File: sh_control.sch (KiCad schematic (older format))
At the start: 0 parts

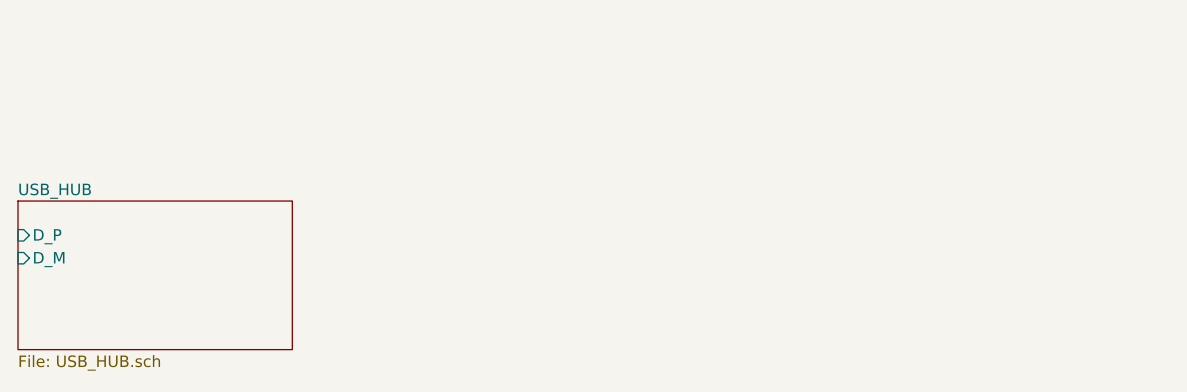
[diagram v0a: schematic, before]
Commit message: added atmega32 schematic
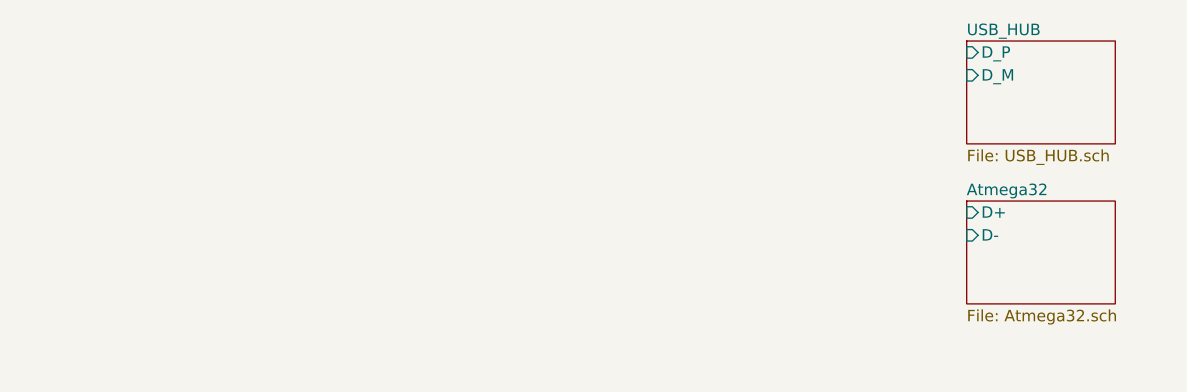
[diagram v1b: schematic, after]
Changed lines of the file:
@@
 $Descr A4 11693 8268
 encoding utf-8
-Sheet 1 2
+Sheet 1 3
 Title ""
 Date ""
@@
 $EndDescr
 $Sheet
-S 1800 2400 1200 650
+S 5950 1700 650  450
 U 61280420
 F0 "USB_HUB" 50
 F1 "USB_HUB.sch" 50
-F2 "D_P" I L 1800 2550 50
-F3 "D_M" I L 1800 2650 50
+F2 "D_P" I L 5950 1750 50
+F3 "D_M" I L 5950 1850 50
+$EndSheet
+$Sheet
+S 5950 2400 650  450
+U 61383560
+F0 "Atmega32" 50
+F1 "Atmega32.sch" 50
+F2 "D+" I L 5950 2450 50
+F3 "D-" I L 5950 2550 50
 $EndSheet
 $EndSCHEMATC

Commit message: file: finished schematic
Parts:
- added C19, C? (x4): 100 uF, symbol Device:C_Small
- added D10, D11, D12, D13, D14: WS2812B, LED_SMD:LED_WS2812B_PLCC4_5.0x5.0mm_P3.2mm, symbol LED:WS2812B
- added D15: LED_Small, symbol Device:LED_Small
- added F1: 500 mA, symbol Device:Fuse
- added J6: C10418, C10418, symbol max_KiCAD_lib:C10418
- added R14: 1.5K, symbol Device:R_Small
- added R?: 300, symbol Device:R_Small
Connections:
- new net: F1.2, J6.1
- new net: D15.2 (A), R14.2
- new net: D10.2 (DOUT), D11.4 (DIN)
- new net: D10.4 (DIN), R?.1
- new net: C?.1, D11.1 (VDD)
- new net: D11.2 (DOUT), D12.4 (DIN)
- new net: C?.1, D13.1 (VDD)
- new net: D13.2 (DOUT), D14.4 (DIN)
- new net: D12.2 (DOUT), D13.4 (DIN)
- new net: C?.1, D14.1 (VDD)
- new net: C?.1, D12.1 (VDD)
- new net +5V: C19.1, D10.1 (VDD), F1.1, R14.1
- new net D_N: J6.2
- new net D_P: J6.3
- new net GND: C19.2, C?.2, C?.2, C?.2, C?.2, D10.3 (VSS), D11.3 (VSS), D12.3 (VSS), D13.3 (VSS), D14.3 (VSS), D15.1 (K), J6.5, J6.6 (MH1), J6.7 (MH2), J6.8 (MH3), J6.9 (MH4)
- new net data: R?.2
- no-connect marks 0 -> 1

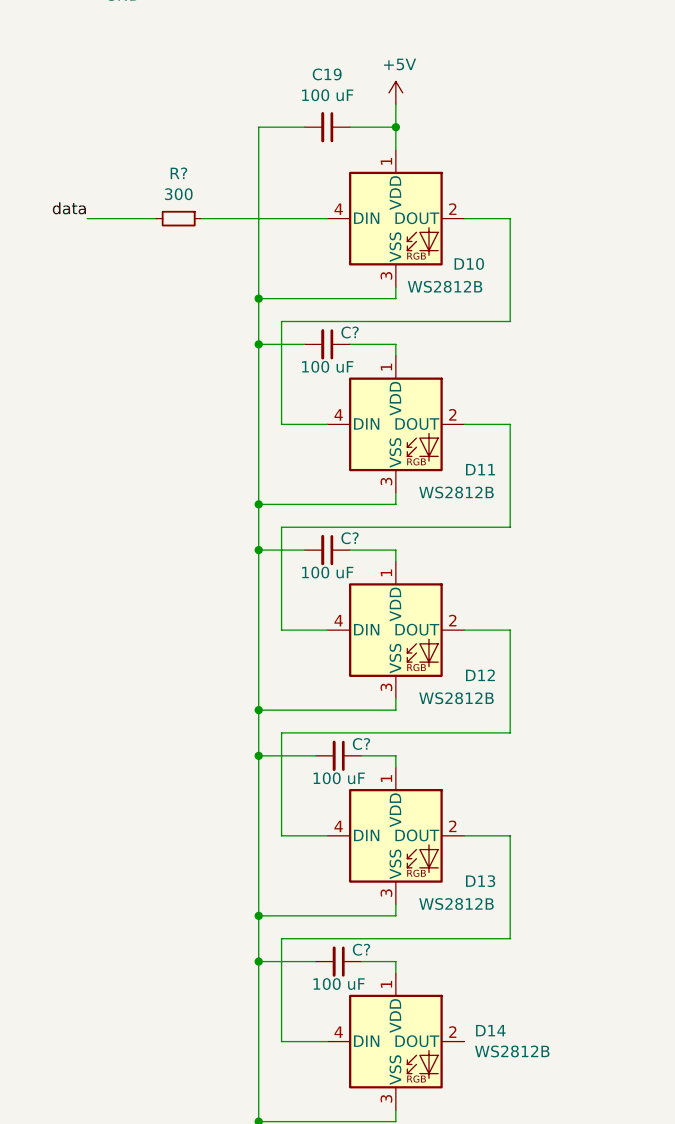
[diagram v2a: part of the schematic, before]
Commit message: small changes to schematic
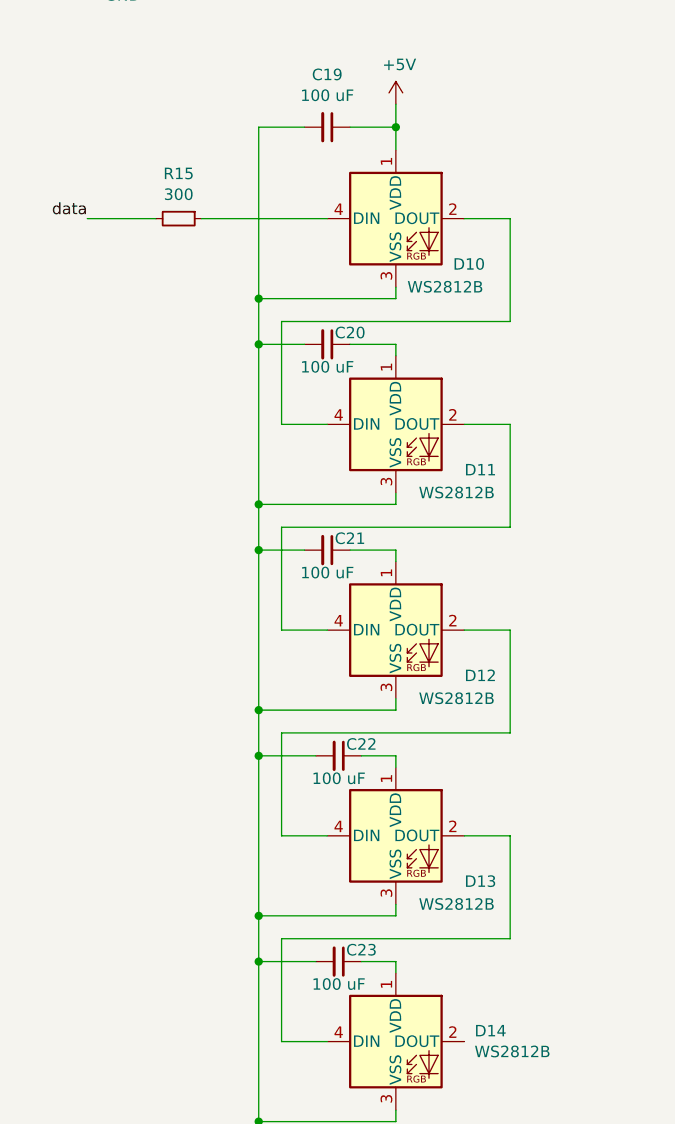
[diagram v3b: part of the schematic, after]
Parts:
- C19: footprint (none) -> Capacitor_SMD:C_1210_3225Metric
- C20, C21, C22, C23: renamed from C?; footprint (none) -> Capacitor_SMD:C_1210_3225Metric
- D15: footprint (none) -> LED_SMD:LED_0603_1608Metric
- F1: footprint (none) -> Fuse:Fuse_1812_4532Metric
- J6: footprint C10418 -> max_KiCAD_lib:C10418
- R14: footprint (none) -> Fuse:Fuse_0603_1608Metric
- R15: renamed from R?; footprint (none) -> Fuse:Fuse_0603_1608Metric
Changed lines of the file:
@@
 F 0 "J6" V 1796 1028 50  0000 L CNN
 F 1 "C10418" V 1705 1028 50  0000 L CNN
-F 2 "C10418" H 2200 1000 50  0001 L CNN
+F 2 "max_KiCAD_lib:C10418" H 2200 1000 50  0001 L CNN
 F 3 "https://datasheet.lcsc.com/szlcsc/Jing-Extension-of-the-Electronic-Co-LCSC-MICRO-USB-5S-B-Type-horns-High-temperature_C10418.pdf" H 2200 900 50  0001 L CNN
 F 4 "USB Connectors SMD RoHS" H 2200 800 50  0001 L CNN "Description"
@@
 F 0 "F1" V 1903 1300 50  0000 C CNN
 F 1 "500 mA" V 1994 1300 50  0000 C CNN
-F 2 "" V 2030 1300 50  0001 C CNN
+F 2 "Fuse:Fuse_1812_4532Metric" V 2030 1300 50  0001 C CNN
 F 3 "~" H 2100 1300 50  0001 C CNN
 	1    2100 1300
@@
 F 0 "D15" V 3246 1530 50  0000 R CNN
 F 1 "LED_Small" V 3155 1530 50  0000 R CNN
-F 2 "" V 3200 1600 50  0001 C CNN
+F 2 "LED_SMD:LED_0603_1608Metric" V 3200 1600 50  0001 C CNN
 F 3 "~" V 3200 1600 50  0001 C CNN
 	1    3200 1600
@@
 F 0 "R14" H 3259 1346 50  0000 L CNN
 F 1 "1.5K" H 3259 1255 50  0000 L CNN
-F 2 "" H 3200 1300 50  0001 C CNN
+F 2 "Fuse:Fuse_0603_1608Metric" H 3200 1300 50  0001 C CNN
 F 3 "~" H 3200 1300 50  0001 C CNN
 	1    3200 1300
@@
 F 0 "C19" V 1821 2950 50  0000 C CNN
 F 1 "100 uF" V 1912 2950 50  0000 C CNN
-F 2 "" H 2050 2950 50  0001 C CNN
+F 2 "Capacitor_SMD:C_1210_3225Metric" H 2050 2950 50  0001 C CNN
 F 3 "~" H 2050 2950 50  0001 C CNN
 	1    2050 2950
@@
 $EndComp
 $Comp
-L Device:R_Small R?
+L Device:R_Small R15
 U 1 1 613AA0B5
 P 1400 3350
-F 0 "R?" V 1204 3350 50  0000 C CNN
+F 0 "R15" V 1204 3350 50  0000 C CNN
 F 1 "300" V 1295 3350 50  0000 C CNN
-F 2 "" H 1400 3350 50  0001 C CNN
+F 2 "Fuse:Fuse_0603_1608Metric" H 1400 3350 50  0001 C CNN
 F 3 "~" H 1400 3350 50  0001 C CNN
 	1    1400 3350
@@
 	1850 6950 2050 6950
 $Comp
-L Device:C_Small C?
+L Device:C_Small C20
 U 1 1 613B5BA4
 P 2050 3900
-F 0 "C?" V 2000 4000 50  0000 C CNN
+F 0 "C20" V 2000 4000 50  0000 C CNN
 F 1 "100 uF" V 2150 3900 50  0000 C CNN
-F 2 "" H 2050 3900 50  0001 C CNN
+F 2 "Capacitor_SMD:C_1210_3225Metric" H 2050 3900 50  0001 C CNN
 F 3 "~" H 2050 3900 50  0001 C CNN
 	1    2050 3900
@@
 	1750 3900 1750 4600
 $Comp
-L Device:C_Small C?
+L Device:C_Small C21
 U 1 1 613BC18D
 P 2050 4800
-F 0 "C?" V 2000 4900 50  0000 C CNN
+F 0 "C21" V 2000 4900 50  0000 C CNN
 F 1 "100 uF" V 2150 4800 50  0000 C CNN
-F 2 "" H 2050 4800 50  0001 C CNN
+F 2 "Capacitor_SMD:C_1210_3225Metric" H 2050 4800 50  0001 C CNN
 F 3 "~" H 2050 4800 50  0001 C CNN
 	1    2050 4800
@@
 	1750 4800 1750 5500
 $Comp
-L Device:C_Small C?
+L Device:C_Small C22
 U 1 1 613BFEA1
 P 2100 5700
-F 0 "C?" V 2050 5800 50  0000 C CNN
+F 0 "C22" V 2050 5800 50  0000 C CNN
 F 1 "100 uF" V 2200 5700 50  0000 C CNN
-F 2 "" H 2100 5700 50  0001 C CNN
+F 2 "Capacitor_SMD:C_1210_3225Metric" H 2100 5700 50  0001 C CNN
 F 3 "~" H 2100 5700 50  0001 C CNN
 	1    2100 5700
@@
 	1750 5700 1750 6400
 $Comp
-L Device:C_Small C?
+L Device:C_Small C23
 U 1 1 613C3B18
 P 2100 6600
-F 0 "C?" V 2050 6700 50  0000 C CNN
+F 0 "C23" V 2050 6700 50  0000 C CNN
 F 1 "100 uF" V 2200 6600 50  0000 C CNN
-F 2 "" H 2100 6600 50  0001 C CNN
+F 2 "Capacitor_SMD:C_1210_3225Metric" H 2100 6600 50  0001 C CNN
 F 3 "~" H 2100 6600 50  0001 C CNN
 	1    2100 6600
@@
 	2350 6600 2350 6650
 $Comp
-L power:+5V #PWR?
+L power:+5V #PWR0150
 U 1 1 613CA1DD
 P 2350 2850
-F 0 "#PWR?" H 2350 2700 50  0001 C CNN
+F 0 "#PWR0150" H 2350 2700 50  0001 C CNN
 F 1 "+5V" H 2365 3023 50  0000 C CNN
 F 2 "" H 2350 2850 50  0001 C CNN
